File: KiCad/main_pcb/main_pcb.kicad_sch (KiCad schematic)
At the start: 18 parts, among them U4 SD Card Socket, U5 TI TXB0104DR, U6 TI TXB0104DR, U7 TI TXB0104DR, U8 CH340C, U9 ILI9488

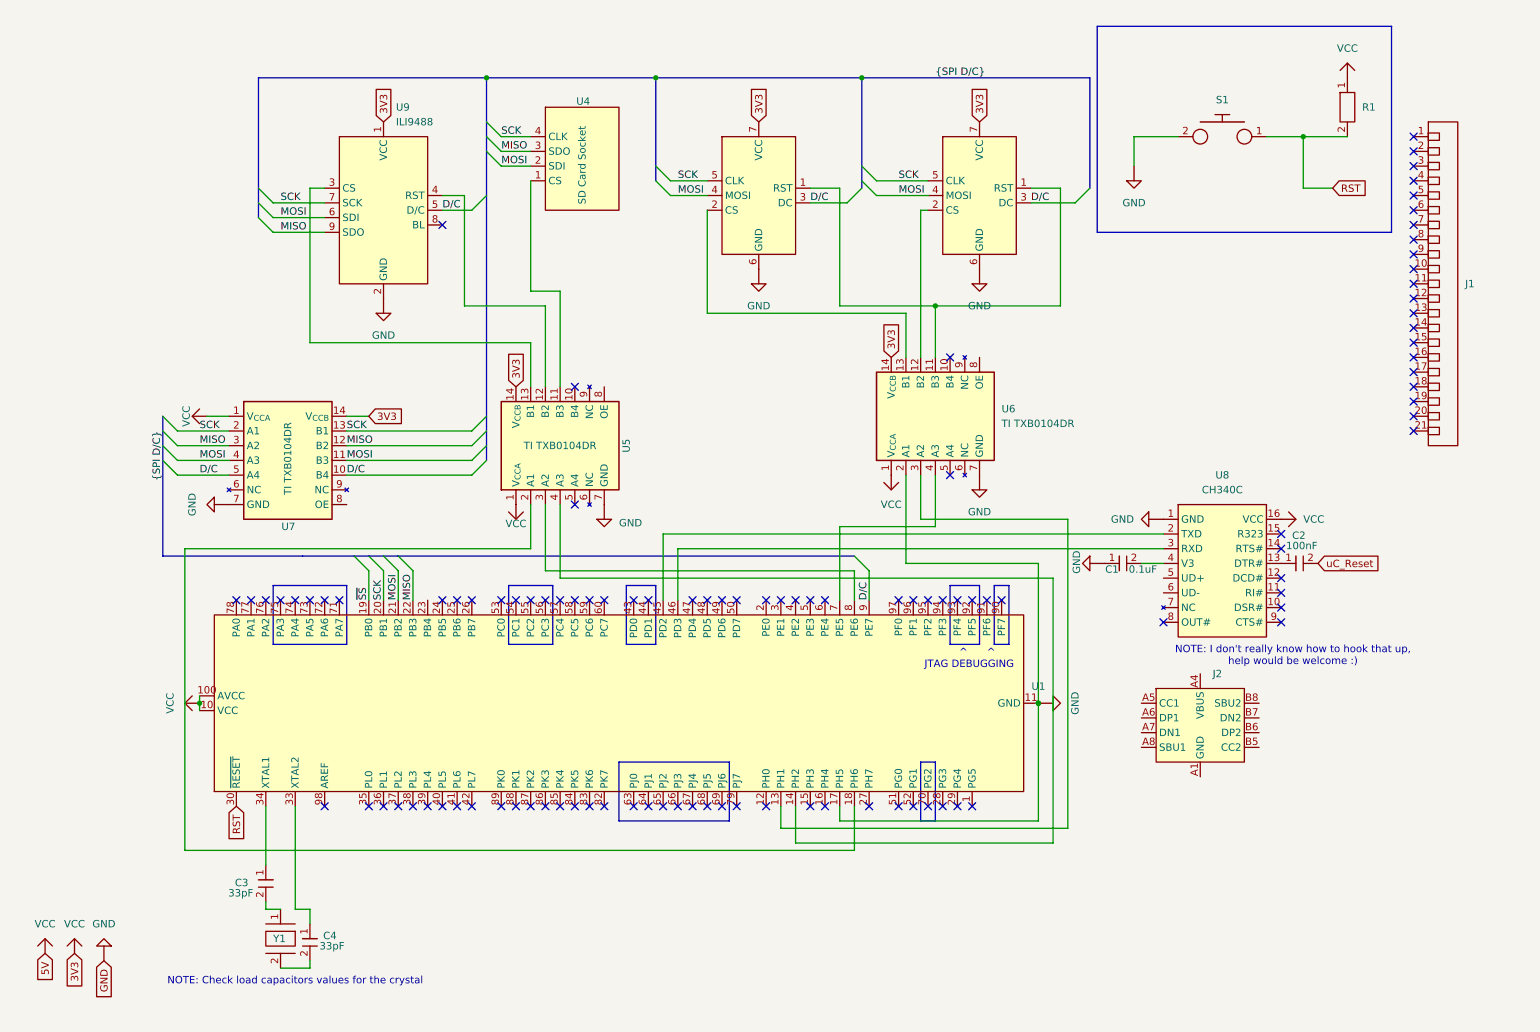
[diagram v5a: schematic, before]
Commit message: feat(KiCad): Continues work on main PCB circuit
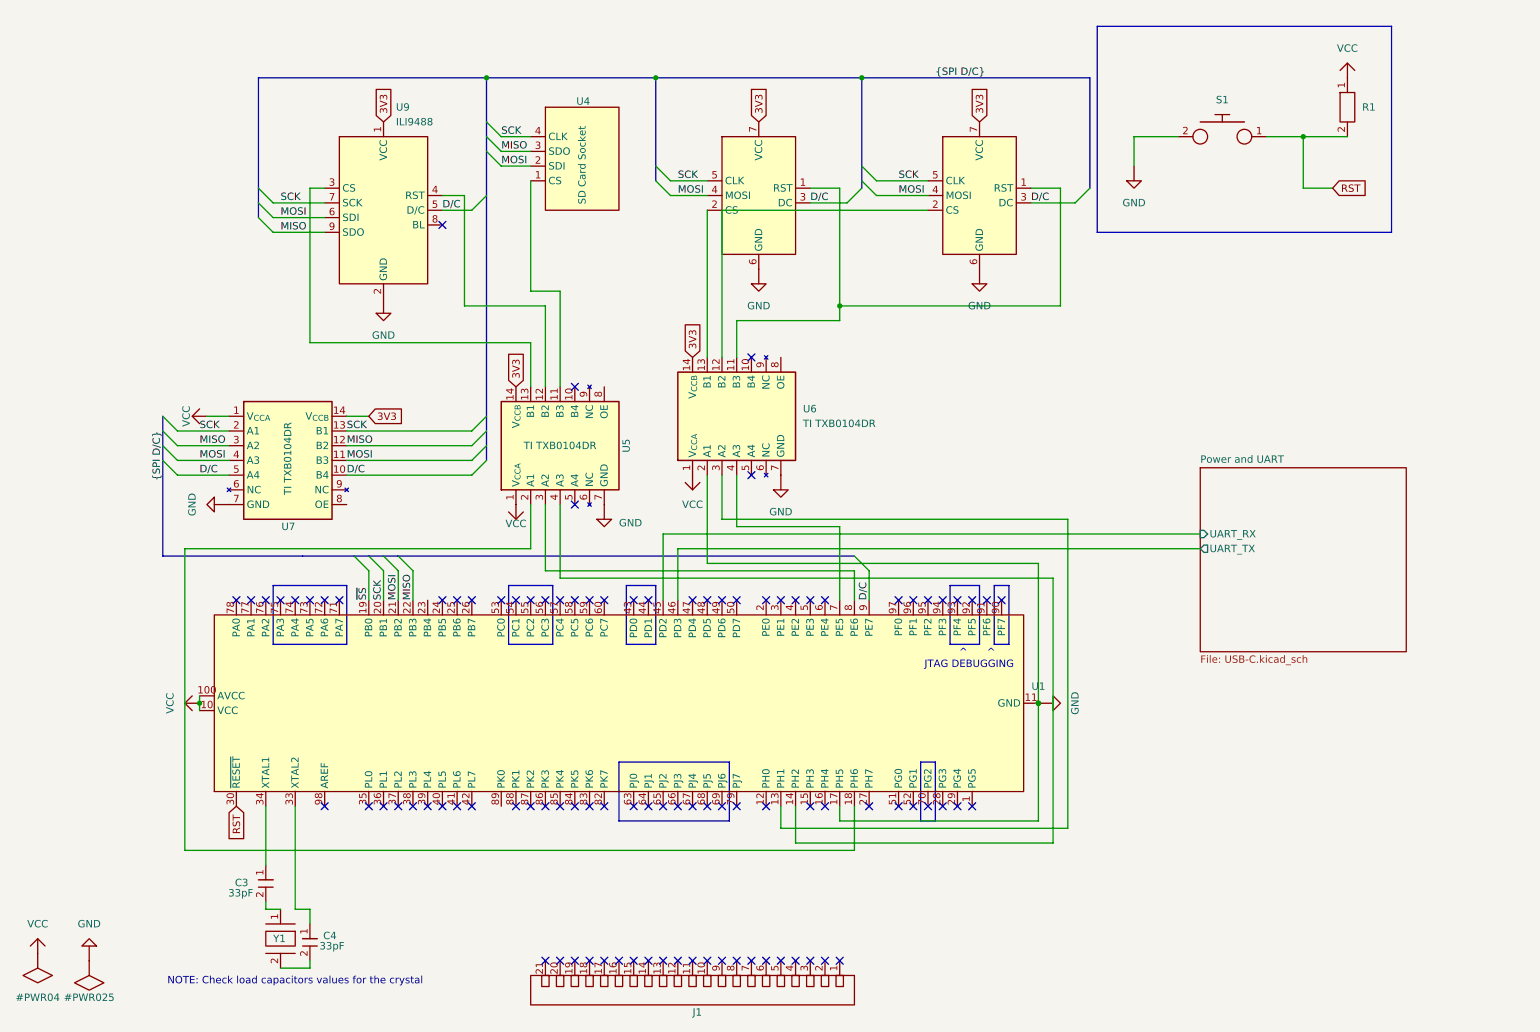
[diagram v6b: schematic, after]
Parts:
- removed C1: 0.1uF, symbol Lily's_Pad:Capacitor
- removed C2: 100nF, symbol Lily's_Pad:Capacitor
- removed J2: (no value), symbol Lily's_Pad:USB_TYPE-C-31-M-14
- removed U8: CH340C, symbol Lily's_Pad:CH340C
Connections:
- net VCC: no longer U2.7 (VCC), U3.7 (VCC), U5.14 (V_{CCB}), U6.14 (V_{CCB}), U7.14 (V_{CCB}), U9.1 (VCC)
- net Power and UART/UART_RX: now reaches U1.45 (PD2)
- net Power and UART/UART_TX: now reaches U1.46 (PD3)
- new net 3V3: U2.7 (VCC), U3.7 (VCC), U5.14 (V_{CCB}), U6.14 (V_{CCB}), U7.14 (V_{CCB}), U9.1 (VCC)
- no-connect marks 106 -> 98
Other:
- added sheet Power and UART (USB-C.kicad_sch)
- note removed: "NOTE: I don't really know how to hook that up, help would be welcome :)"
- moved on the sheet: J1, U6

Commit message: feat(KiCad): Continues work on main PCB circuit
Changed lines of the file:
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@@
+		)
+	)
+	(global_label "3V3"
+		(shape input)
+		(at 33.02 182.88 90)
+		(fields_autoplaced yes)
+		(effects
+			(font
+				(size 1.27 1.27)
+			)
+			(justify left)
+		)
+		(property "Intersheetrefs" "${INTERSHEET_REFS}"
+			(at 33.02 176.3872 90)
+			(hide yes)
+			(show_name no)
+			(do_not_autoplace no)
+			(effects
+				(font
+					(size 1.27 1.27)
+				)
+				(justify left)
+			)
 		)
 	)
@@
 	(symbol
 		(lib_id "Lily's_Pad:GC9A01")
-		(at 173.99 45.72 0)
+		(at 180.34 53.34 0)
 		(unit 1)
 		(body_style 1)
@@
 		(fields_autoplaced yes)
 		(property "Reference" "U2"
-			(at 182.4833 40.64 0)
+			(at 188.8333 48.26 0)
 			(hide yes)
 			(show_name no)
@@
 		)
 		(property "Value" ""
-			(at 173.99 45.72 0)
-			(show_name no)
-			(do_not_autoplace no)
-			(effects
-				(font
-					(size 1.27 1.27)
-				)
-			)
-		)
-		(property "Footprint" ""
-			(at 173.99 45.72 0)
-			(hide yes)
-			(show_name no)
-			(do_not_autoplace no)
-			(effects
-				(font
-					(size 1.27 1.27)
-				)
-			)
-		)
-		(property "Datasheet" ""
-			(at 173.99 45.72 0)
-			(hide yes)
-			(show_name no)
-			(do_not_autoplace no)
-			(effects
-				(font
-					(size 1.27 1.27)
-				)
-			)
-		)
-		(property "Description" ""
-			(at 173.99 45.72 0)
+			(at 180.34 53.34 0)
+			(show_name no)
+			(do_not_autoplace no)
+			(effects
+				(font
+					(size 1.27 1.27)
+				)
+			)
+		)
+		(property "Footprint" ""
+			(at 180.34 53.34 0)
+			(hide yes)
+			(show_name no)
+			(do_not_autoplace no)
+			(effects
+				(font
+					(size 1.27 1.27)
+				)
+			)
+		)
+		(property "Datasheet" "file:///Users/apetitco/Documents/Module Elec - Lily's Pad/Datasheets/U - Integrated Circuits/Screen Drivers/GC9A01A.pdf"
+			(at 180.34 53.34 0)
+			(hide yes)
+			(show_name no)
+			(do_not_autoplace no)
+			(effects
+				(font
+					(size 1.27 1.27)
+				)
+			)
+		)
+		(property "Description" ""
+			(at 180.34 53.34 0)
 			(hide yes)
 			(show_name no)
@@
 	(symbol
 		(lib_id "Lily's_Pad:GC9A01")
-		(at 135.89 45.72 0)
+		(at 142.24 53.34 0)
 		(unit 1)
 		(body_style 1)
@@
 		(fields_autoplaced yes)
 		(property "Reference" "U3"
-			(at 144.3833 40.64 0)
+			(at 150.7333 48.26 0)
 			(hide yes)
 			(show_name no)
@@
 		)
 		(property "Value" ""
-			(at 135.89 45.72 0)
-			(show_name no)
-			(do_not_autoplace no)
-			(effects
-				(font
-					(size 1.27 1.27)
-				)
-			)
-		)
-		(property "Footprint" ""
-			(at 135.89 45.72 0)
-			(hide yes)
-			(show_name no)
-			(do_not_autoplace no)
-			(effects
-				(font
-					(size 1.27 1.27)
-				)
-			)
-		)
-		(property "Datasheet" ""
-			(at 135.89 45.72 0)
-			(hide yes)
-			(show_name no)
-			(do_not_autoplace no)
-			(effects
-				(font
-					(size 1.27 1.27)
-				)
-			)
-		)
-		(property "Description" ""
-			(at 135.89 45.72 0)
+			(at 142.24 53.34 0)
+			(show_name no)
+			(do_not_autoplace no)
+			(effects
+				(font
+					(size 1.27 1.27)
+				)
+			)
+		)
+		(property "Footprint" ""
+			(at 142.24 53.34 0)
+			(hide yes)
+			(show_name no)
+			(do_not_autoplace no)
+			(effects
+				(font
+					(size 1.27 1.27)
+				)
+			)
+		)
+		(property "Datasheet" "file:///Users/apetitco/Documents/Module Elec - Lily's Pad/Datasheets/U - Integrated Circuits/Screen Drivers/GC9A01A.pdf"
+			(at 142.24 53.34 0)
+			(hide yes)
+			(show_name no)
+			(do_not_autoplace no)
+			(effects
+				(font
+					(size 1.27 1.27)
+				)
+			)
+		)
+		(property "Description" ""
+			(at 142.24 53.34 0)
 			(hide yes)
 			(show_name no)
@@
 					(unit 1)
 				)
+			)
+		)
+	)
+	(symbol
+		(lib_id "Lily's_Pad:PWR_FLG")
+		(at 33.02 185.42 0)
+		(unit 1)
+		(body_style 1)
+		(exclude_from_sim no)
+		(in_bom no)
+		(on_board no)
+		(in_pos_files yes)
+		(dnp no)
+		(fields_autoplaced yes)
+		(property "Reference" "#PWR026"
+			(at 33.02 185.42 0)
+			(hide yes)
+			(show_name no)
+			(do_not_autoplace no)
+			(effects
+				(font
+					(size 1.27 1.27)
+				)
+			)
+		)
+		(property "Value" "PWR_FLG"
+			(at 33.02 185.42 0)
+			(hide yes)
+			(show_name no)
+			(do_not_autoplace no)
+			(effects
+				(font
+					(size 1.27 1.27)
+				)
+			)
+		)
+		(property "Footprint" ""
+			(at 33.02 185.42 0)
+			(hide yes)
+			(show_name no)
+			(do_not_autoplace no)
+			(effects
+				(font
+					(size 1.27 1.27)
+				)
+			)
+		)
+		(property "Datasheet" ""
+			(at 33.02 185.42 0)
+			(hide yes)
+			(show_name no)
+			(do_not_autoplace no)
+			(effects
+				(font
+					(size 1.27 1.27)
+				)
+			)
+		)
+		(property "Description" ""
+			(at 33.02 185.42 0)
+			(hide yes)
+			(show_name no)
+			(do_not_autoplace no)
+			(effects
+				(font
+					(size 1.27 1.27)
+				)
+			)
+		)
+		(pin "1"
+		)
+		(instances
+			(project "main_pcb"
+				(path "/346fb29b-2426-4b69-9f9a-e979b6e41832"
+					(reference "#PWR026")
+					(unit 1)
+				)

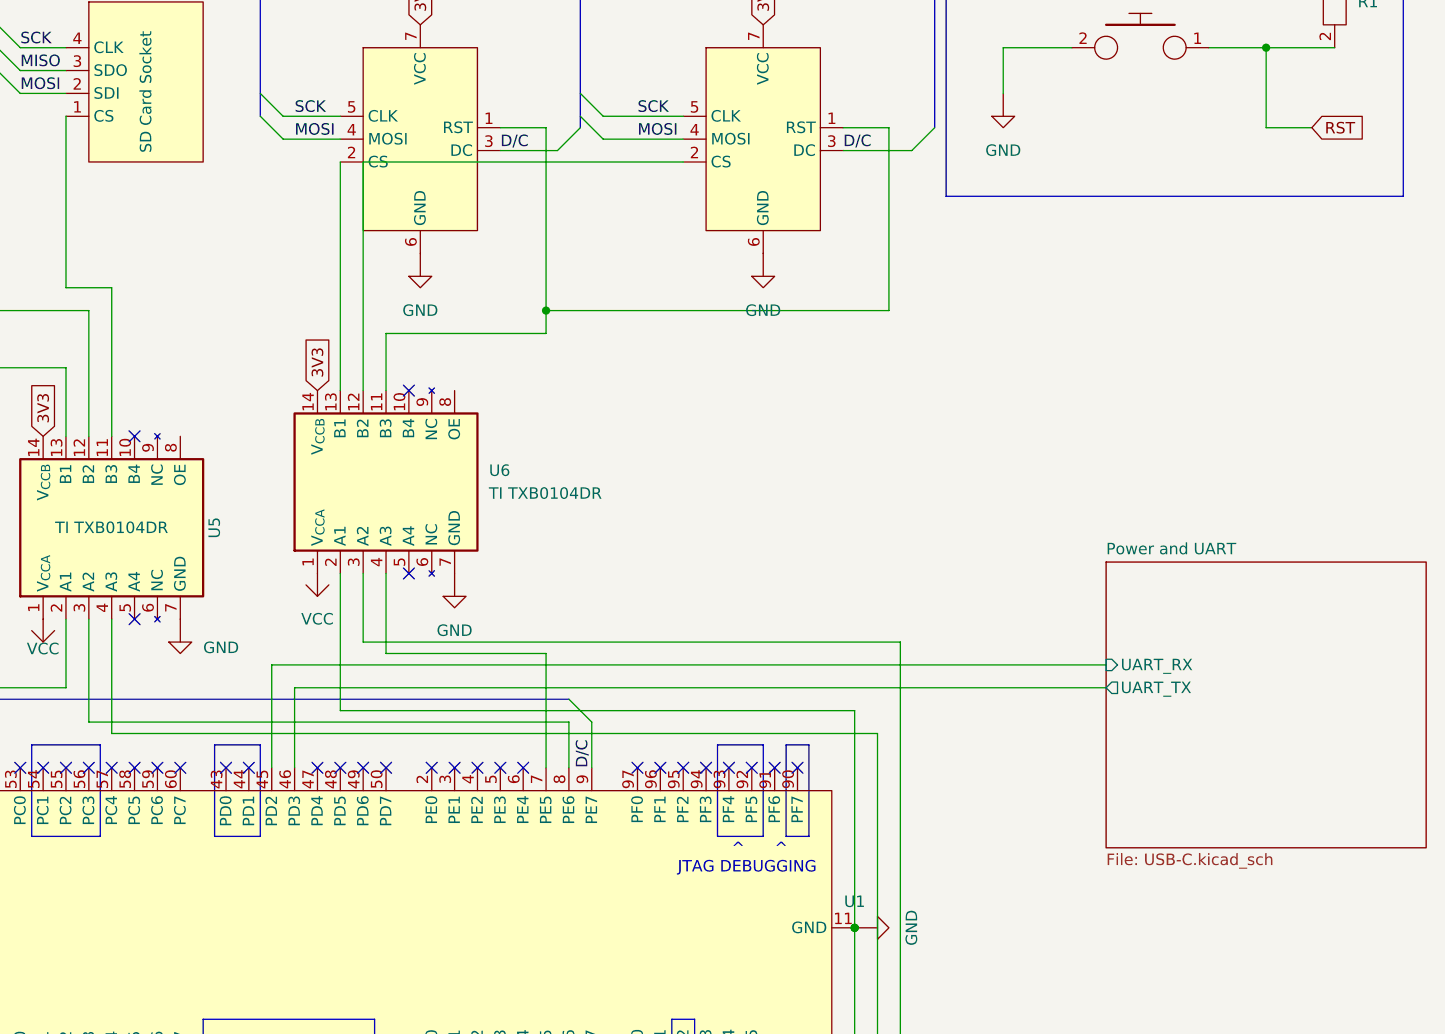
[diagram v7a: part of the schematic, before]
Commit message: feat(KiCad): Continues work on main PCB circuit
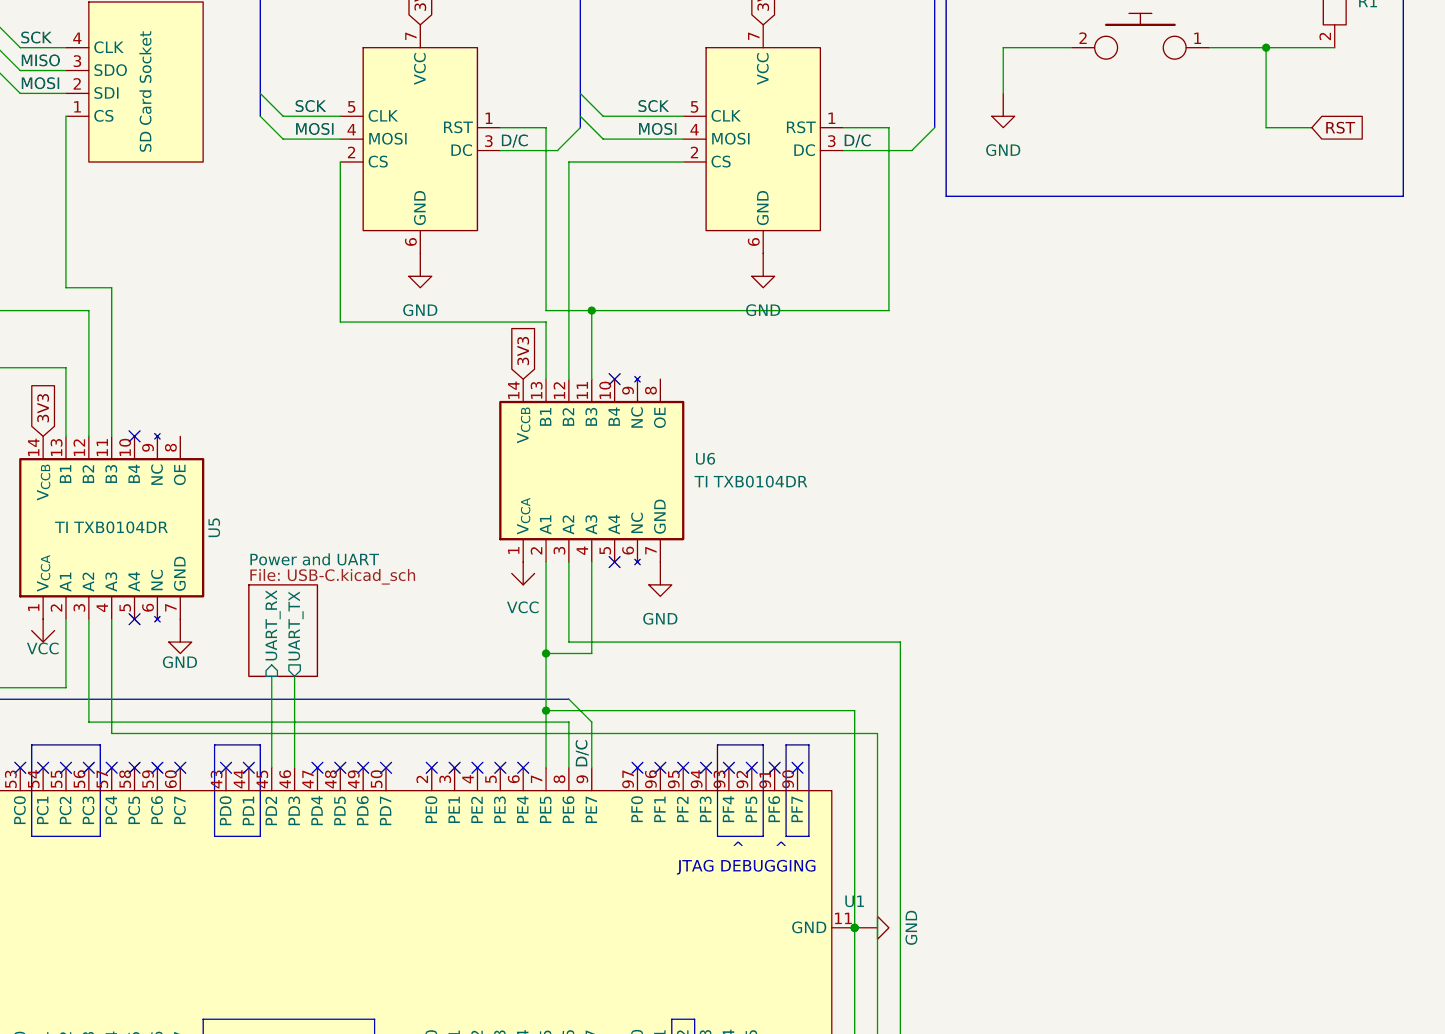
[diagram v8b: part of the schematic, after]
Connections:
- net GND: now also U1.7 (PE5), U6.4 (A3)
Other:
- moved on the sheet: U6
